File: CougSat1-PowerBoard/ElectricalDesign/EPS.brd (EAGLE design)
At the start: 91.4 x 95.8 mm, 250 parts, among them J1 PV0, J2 PV1, J3 PV2, J4 PV3, J5 Umbilical, J6 SWD, J7 CougSat Card, J8 Deployables, Q1 NTLUD3A50PZ, Q10 DMN2008LFU, Q11 DMN2008LFU, Q12 CSD25402Q3A, Q13 CSD25402Q3A, Q14 NTLUD3A50PZ, Q15 NTLUD3A50PZ, Q16 NTLUD3A50PZ, Q17 NTLUD3A50PZ, Q18 NTLUD3A50PZ, Q19 NTLUD3A50PZ, Q2 NTLUD3A50PZ, Q20 NTLUD3A50PZ, Q21 NTLUD3A50PZ, Q22 NTLUD3A50PZ, Q23 CSD25402Q3A, Q24 CSD25402Q3A, Q25 DMN53D0L, Q26 NTLUD3A50PZ, Q27 NTLUD3A50PZ, Q28 NTLUD3A50PZ, Q29 NTLUD3A50PZ, Q3 NTLUD3A50PZ, Q30 NTLUD3A50PZ, Q31 NTLUD3A50PZ, Q32 NTLUD3A50PZ, Q33 NTLUD3A50PZ, Q34 NTLUD3A50PZ, Q35 NTLUD3A50PZ, Q36 NTLUD3A50PZ, Q37 NTLUD3A50PZ, Q38 NTLUD3A50PZ, Q39 NTLUD3A50PZ, Q4 NTLUD3A50PZ, Q40 NTLUD3A50PZ, Q41 NTLUD3A50PZ, Q42 NTLUD3A50PZ, Q43 NTLUD3A50PZ, Q5 NTLUD3A50PZ, Q6 NTLUD3A50PZ, Q7 NTLUD3A50PZ, Q8 NTLUD3A50PZ, Q9 NTLUD3A50PZ, SW1 D2MQ-1-TL, U1 BQ29700, U10 LTC2499, U11 LTC2499, U12 LTC2499, U13 LTC2499, U14 MCP1501-18, U15 LTC2499, U2 BQ29700, U3 TPS64200, U4 TPS64200, U5 STM32L476RGT, U6 TCA9535R, U7 SN74LVC244AR, U8 TCA9535R, U9 LTC2499

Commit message: Updated I²C Addresses
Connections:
- net 3.3V: no longer U13.36
- net DGND: now also U12.36, U12.37, U13.37; no longer U12.38, U13.38
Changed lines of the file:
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@@
 <drawing>
 <settings>
-<setting alwaysvectorfont="yes"/>
+<setting alwaysvectorfont="no"/>
 <setting verticaltext="up"/>
 </settings>
@@
 <contactref element="C41" pad="2"/>
 <contactref element="R77" pad="1"/>
-<contactref element="U12" pad="38"/>
-<contactref element="U13" pad="38"/>
 <wire x1="21.3" y1="38.45" x2="18.9" y2="38.45" width="0.16" layer="16"/>
 <wire x1="18.9" y1="38.45" x2="18.9" y2="38.2" width="0.16" layer="16"/>
@@
 <wire x1="30.805" y1="-6.635" x2="30.8" y2="-6.635" width="0.3" layer="16"/>
 <wire x1="30.8" y1="-6.635" x2="29.8" y2="-6.635" width="0.16" layer="16"/>
+<contactref element="U12" pad="36"/>
+<contactref element="U12" pad="37"/>
+<contactref element="U13" pad="37"/>
 <wire x1="56.3" y1="28.8" x2="57.2" y2="28.15" width="0" layer="19" extent="16-16"/>
 <wire x1="55.8" y1="28.8" x2="56.3" y2="28.8" width="0" layer="19" extent="16-16"/>
@@
 <wire x1="34.14" y1="-5.575" x2="42.2" y2="-3.965" width="0" layer="19" extent="16-16"/>
 <wire x1="44.7" y1="-19.05" x2="50.8" y2="-10.465" width="0" layer="19" extent="16-16"/>
-<wire x1="43.8" y1="-18.4" x2="44.7" y2="-19.05" width="0" layer="19" extent="16-16"/>
 <wire x1="44.7" y1="-20.55" x2="44.7" y2="-19.05" width="0" layer="19" extent="16-16"/>
 <wire x1="44.7" y1="-21.55" x2="44.7" y2="-20.55" width="0" layer="19" extent="16-16"/>
-<wire x1="42.3" y1="-18.4" x2="43.8" y2="-18.4" width="0" layer="19" extent="16-16"/>
+<wire x1="43.3" y1="-18.4" x2="44.7" y2="-19.05" width="0" layer="19" extent="16-16"/>
+<wire x1="42.8" y1="-18.4" x2="43.3" y2="-18.4" width="0" layer="19" extent="16-16"/>
+<wire x1="42.3" y1="-18.4" x2="42.8" y2="-18.4" width="0" layer="19" extent="16-16"/>
 <wire x1="41.8" y1="-18.4" x2="42.3" y2="-18.4" width="0" layer="19" extent="16-16"/>
 <wire x1="41.3" y1="-18.4" x2="41.8" y2="-18.4" width="0" layer="19" extent="16-16"/>
@@
 <wire x1="34.4" y1="-36.5" x2="33.9" y2="-36.5" width="0" layer="19" extent="16-16"/>
 <wire x1="34.9" y1="-36.5" x2="34.4" y2="-36.5" width="0" layer="19" extent="16-16"/>
+<wire x1="35.9" y1="-36.5" x2="34.9" y2="-36.5" width="0" layer="19" extent="16-16"/>
 <wire x1="32.5" y1="-37.15" x2="33.4" y2="-36.5" width="0" layer="19" extent="16-16"/>
-<wire x1="36.4" y1="-36.5" x2="34.9" y2="-36.5" width="0" layer="19" extent="16-16"/>
-<wire x1="37.3" y1="-37.15" x2="36.4" y2="-36.5" width="0" layer="19" extent="16-16"/>
+<wire x1="37.3" y1="-37.15" x2="35.9" y2="-36.5" width="0" layer="19" extent="16-16"/>
 <wire x1="37.3" y1="-38.65" x2="37.3" y2="-37.15" width="0" layer="19" extent="16-16"/>
 <wire x1="37.3" y1="-39.65" x2="37.3" y2="-38.65" width="0" layer="19" extent="16-16"/>
@@
 <contactref element="C20" pad="1"/>
 <contactref element="C37" pad="1"/>
-<contactref element="U13" pad="36"/>
 <contactref element="RN19" pad="5"/>
 <contactref element="RN19" pad="8"/>
@@
 <wire x1="48.95" y1="-23.4" x2="48.235" y2="-21.5" width="0" layer="19" extent="16-16"/>
 <wire x1="35.965" y1="-34.2" x2="39.9" y2="-20.55" width="0" layer="19" extent="16-16"/>
-<wire x1="35.4" y1="-36.5" x2="35.965" y2="-34.2" width="0" layer="19" extent="16-16"/>
-<wire x1="32.5" y1="-38.65" x2="35.4" y2="-36.5" width="0" layer="19" extent="16-16"/>
+<wire x1="32.5" y1="-38.65" x2="35.965" y2="-34.2" width="0" layer="19" extent="16-16"/>
 <wire x1="27.365" y1="-36.9" x2="32.5" y2="-38.65" width="0" layer="19" extent="16-16"/>
 <wire x1="19.3" y1="-35.6" x2="27.365" y2="-36.9" width="0" layer="19" extent="16-16"/>

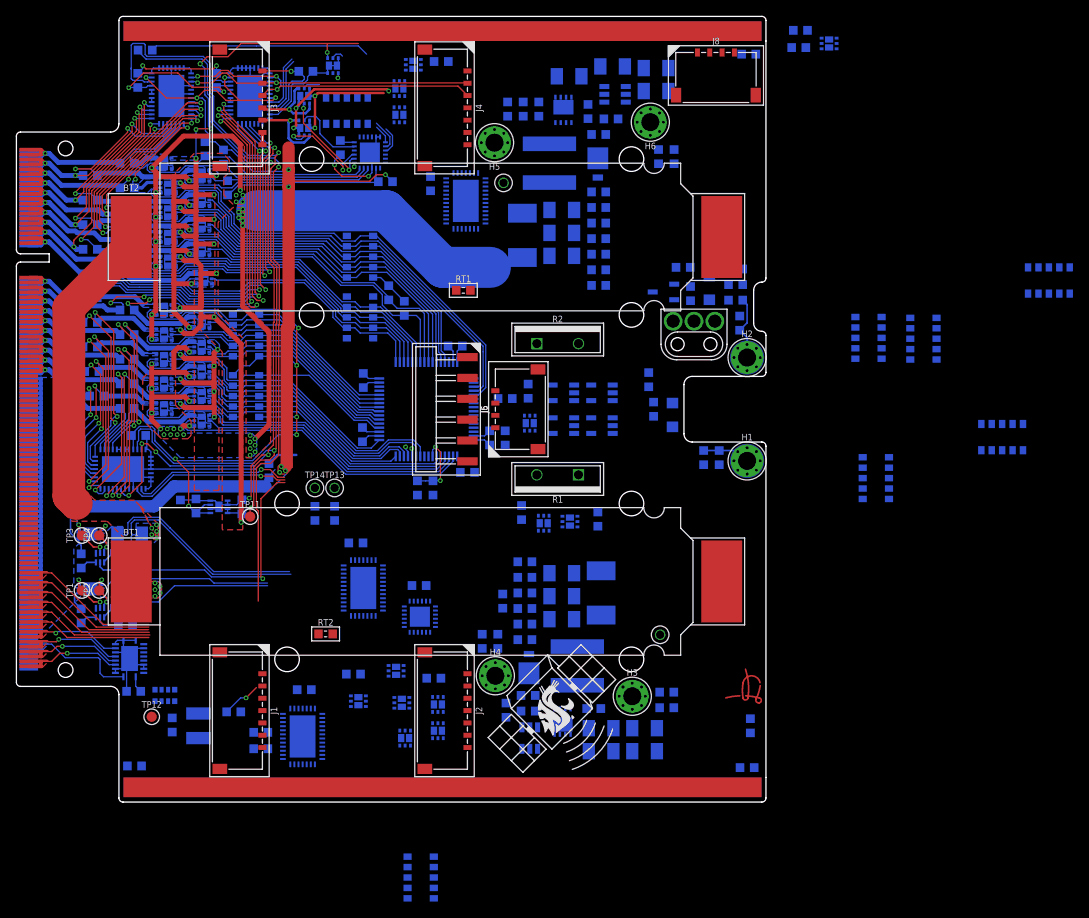
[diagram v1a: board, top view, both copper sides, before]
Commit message: Laid Out Voltage ADC
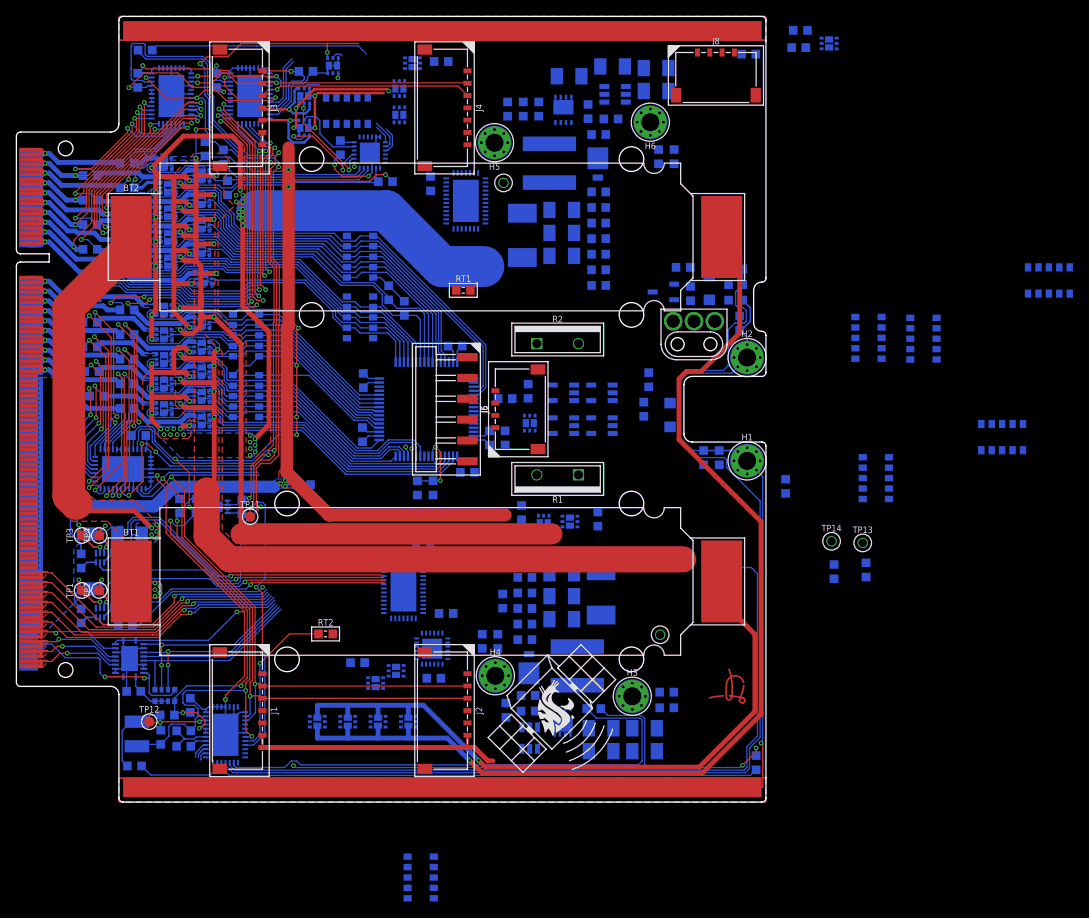
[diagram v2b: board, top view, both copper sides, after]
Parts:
- moved R72 65.2 mm to (103.6, -19.6)
- moved TP13 64.7 mm to (103.2, -16.3)
- moved R71 63.7 mm to (99.7, -19.8)
- moved TP14 63.3 mm to (99.4, -16.1)
- moved R61 29.5 mm to (93.8, -9.40), turned to 90 degrees
- moved C30 14.0 mm to (21.2, -36.1), turned to 90 degrees
- moved Q1 10.6 mm to (36.7, -38.1)
- moved R65 9.40 mm to (20.4, -41.1)
- moved R63 9.40 mm to (20.4, -39.2)
- moved U13 9.40 mm to (25.5, -39.7)
- moved C29 8.23 mm to (49.6, -17.0)
- moved FB1 8.11 mm to (18.4, -37.3)
- moved C36 7.57 mm to (14.7, -39.6)
- moved Q4 7.38 mm to (44.1, -38.1), turned to 0 degrees
- moved Q2 7.28 mm to (40.4, -38.1), turned to 0 degrees
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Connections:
- net 3.3V-A: now also U13.21
- net 3.3V-B: now also U13.22
- net AVREF: now also U13.9
- net EJECT_TIMER: now also U13.16
- net PC_DEPLOY-A: now also U5.56
- net PC_DEPLOY-B: now also U5.57
- net TEMP+X+Y: now also U13.10
- net TEMP+X-Y: now also U13.17
- net TEMP-BATT-A: now also U13.8
- net TEMP-BATT-B: now also U13.19
- net TEMP-PMIC: now also U13.12
- net TEMP-REG-A: now also U13.14
- net TEMP-REG-B: now also U13.23
- net TEMP-X+Y: now also U13.13
- net TEMP-X-Y: now also U13.18
- net UMB_IN: now also U13.11
- net UMB_SW-A: now also U5.59
- net UMB_SW-B: now also U5.58
- net VBATT-A: now also U13.15
- net VBATT-B: now also U13.20
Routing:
- net VBATT-A: track 21.4 -> 189.6 mm
- net CHASSIS: track 13.8 -> 158.4 mm, vias 0 -> 1
- net EJECT_TIMER: track 0.00 -> 140.5 mm
- net VIN-B: track 48.3 -> 174.8 mm, vias 4 -> 5
- net VIN-A: track 16.0 -> 116.7 mm, vias 2 -> 4
- net AVDD: track 87.6 -> 161.3 mm, vias 2 -> 6
- net PGND: track 221.5 -> 288.2 mm
- net TEMP+X-Y: track 0.00 -> 66.5 mm
- net TEMP-REG-A: track 0.00 -> 63.3 mm
- net DGND: track 120.1 -> 179.8 mm, vias 5 -> 8
- net I2C_SDA: track 55.5 -> 112.9 mm, vias 3 -> 4
- net AGND: track 119.3 -> 176.3 mm, vias 10 -> 13
- net I2C_SCL: track 59.4 -> 116.4 mm, vias 4 -> 5
- net 3.3V: track 106.8 -> 157.0 mm, vias 9 -> 13
- net 3.3V-A: track 113.2 -> 153.9 mm, vias 18 -> 17
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- added copper zone on layer 1, net CHASSIS

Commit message: Laid Out 3V3A Regulator
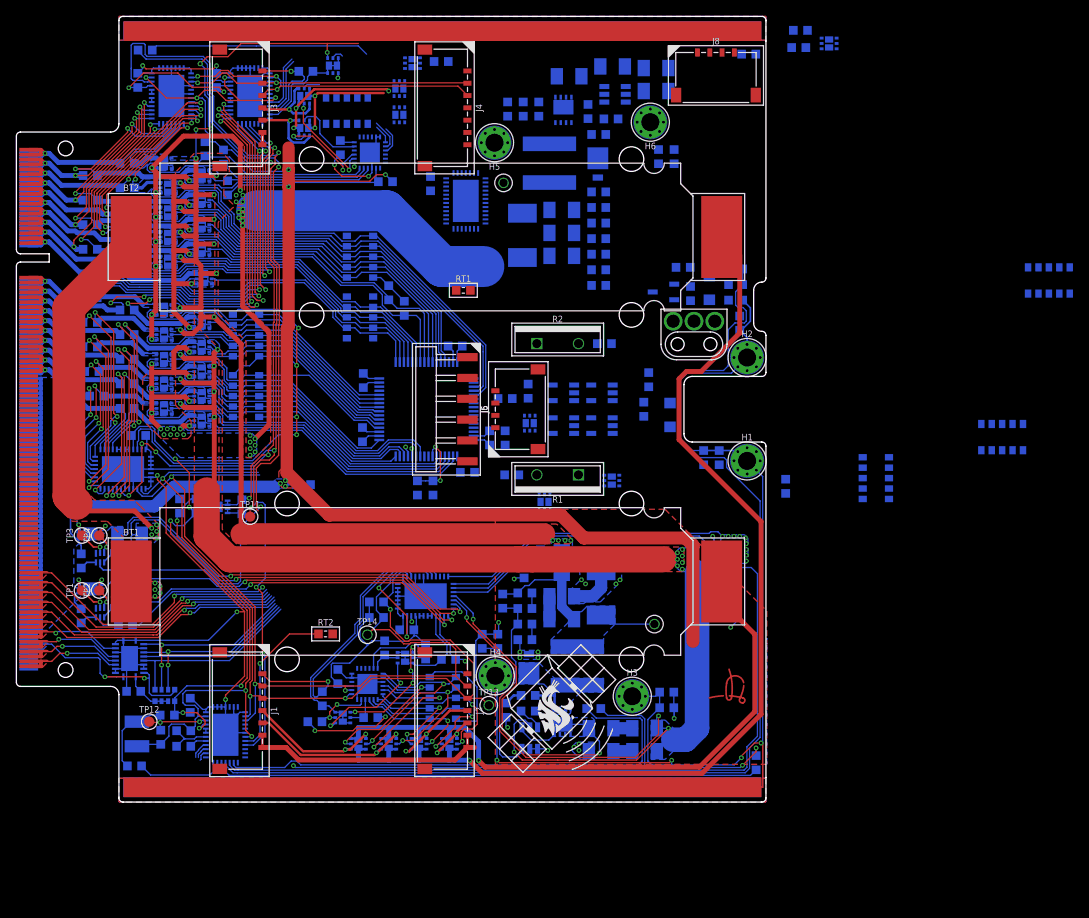
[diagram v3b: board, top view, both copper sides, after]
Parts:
- removed RN4, RN5: 10kΩ 5%, CougsInSpace-Resistors:3264
- added R86, R87, R88, R89: 10kΩ 0.1%, CougsInSpace-Resistors:1608
- moved R72 59.8 mm to (43.9, -23.5), turned to 0 degrees
- moved TP14 57.7 mm to (42.8, -27.5)
- moved R71 56.1 mm to (43.9, -25.4), turned to 0 degrees
- moved TP13 49.7 mm to (57.6, -36.1)
- moved RN20 22.1 mm to (52.0, -35.2)
- moved R57 21.4 mm to (71.7, 8.00), turned to 180 degrees
- moved C23 15.3 mm to (39.2, -32.6), turned to 90 degrees
- moved C29 10.1 mm to (47.6, -26.9)
- moved Q4 9.11 mm to (52.8, -40.8)
- moved U8 8.99 mm to (42.8, -33.5), turned to 270 degrees
- moved Q43 7.14 mm to (72.6, -8.70)
- moved R42 6.15 mm to (37.3, -35.3), turned to 270 degrees
- moved Q28 5.80 mm to (39.8, -37.6)
- moved Q1 5.68 mm to (41.7, -40.8)
- moved Q2 5.68 mm to (45.4, -40.8)
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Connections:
- net 3.3V: now also R86.2, R87.2, R88.2, R89.2; no longer RN4.10, RN4.5, RN5.10, RN5.5
- net 3.3V-A: now also U12.14
- net 3.3V_I-A: now also U12.15
- net 3.3V_ISENS-A: now also U12.16
- net BP_VSS-A: now also U12.21
- net BP_VSS-B: now also U12.19
- net BP_VSS_I-A: now also U12.20
- net BP_VSS_I-B: now also U12.18
- net I_BH-0: now also U12.11
- net PR_BH-0: now also U12.10
- net PVC_3.3V-0A: now also R86.1, U8.16
- net PVC_3.3V-0B: now also R87.1, U8.17
- net PVC_3.3V-1A: now also R88.1, U8.5
- net PVC_3.3V-1B: now also R89.1, U8.6
- net PVI_3.3V-0: now also U12.9
- net PVI_3.3V-1: now also U12.23
- net PV_3.3V-0: now also U12.8
- net PV_3.3V-1: now also U12.22
- net PV_SW-0A: now also U8.7
- net PV_SW-0B: now also RN20.9, U8.8; no longer RN20.2
- net PV_SW-1A: now also RN20.2, U8.10; no longer RN20.3
- net PV_SW-1B: now also RN20.8, U8.11; no longer RN20.4
- net PV_SW-2A: now also U8.15
- net PV_SW-2B: now also U8.13
- net PV_SW-3A: now also RN20.3, U8.12; no longer RN20.8
- net PV_SW-3B: now also RN20.4, U8.14; no longer RN20.9
- net VBATT-A: now also U12.13, U12.17
- net VIN-A: now also U12.12
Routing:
- net VBATT-A: track 189.6 -> 320.2 mm, vias 7 -> 18
- net PGND: track 288.2 -> 368.3 mm, vias 6 -> 23
- net CHASSIS: track 158.4 -> 224.0 mm, vias 1 -> 4
- net 3.3V_ISENS-A: track 0.00 -> 45.7 mm, vias 0 -> 2
- net 3.3V: track 157.0 -> 195.4 mm, vias 13 -> 15
- net 3.3V_I-A: track 0.00 -> 37.0 mm
- net PV_3.3V-0: track 0.00 -> 36.8 mm, vias 0 -> 1
- net VIN-A: track 116.7 -> 151.8 mm, vias 4 -> 13
- net PVI_3.3V-0: track 0.00 -> 33.5 mm
- net I2C_SCL: track 116.4 -> 148.3 mm, vias 5 -> 7
- net I2C_SDA: track 112.9 -> 143.0 mm, vias 4 -> 5
- net 3.3V-A: track 153.9 -> 182.5 mm, vias 17 -> 25
- net DGND: track 179.8 -> 205.7 mm
- net 3.3V_REG_FB-A: track 0.00 -> 24.4 mm
- net PV_SW-0A: track 0.00 -> 22.8 mm, vias 0 -> 2
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- added copper zone on layer 16, net 3.3V_I-A
- added copper zone on layer 16, net 3.3V_ISENS-A
- added copper zone on layer 16, net 3.3V_REG_BUCK_NODE-A
- added copper zone on layer 16, net VIN-A

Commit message: Laid Out Voltage ADC
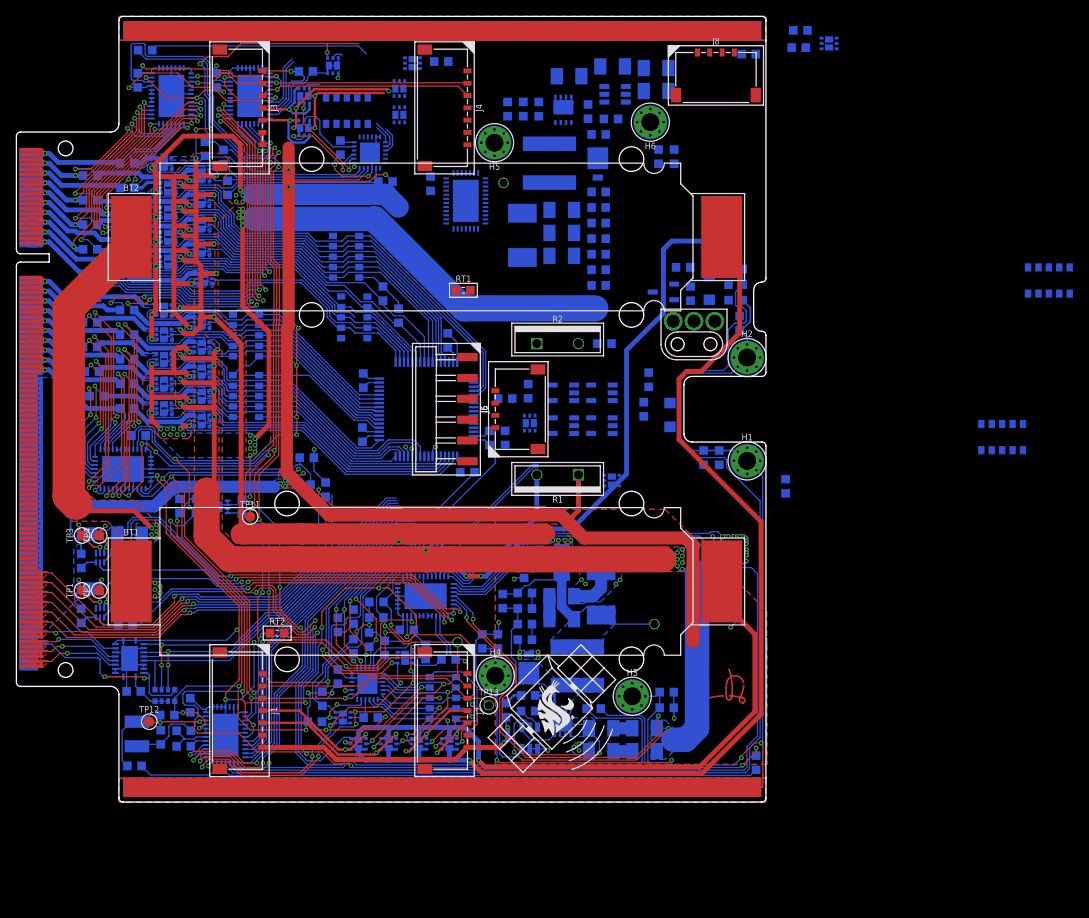
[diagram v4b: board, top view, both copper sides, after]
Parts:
- removed RN6: 10kΩ 5%, CougsInSpace-Resistors:3264
- added R90, R91, R92, R93: 10kΩ 0.1%, CougsInSpace-Resistors:1608
- TP1: value (none) -> TEST_POINT-SMD-C-1.25
- moved C22 15.8 mm to (35.4, -5.90), turned to 0 degrees
- moved Q42 14.5 mm to (51.3, -17.4)
- moved R78 11.2 mm to (37.7, -9.80)
- moved TP14 11.0 mm to (53.8, -28.4), flipped to the bottom
- moved R56 11.0 mm to (54.6, -17.3), turned to 0 degrees
- moved RT2 5.90 mm to (31.8, -27.3)
- moved RN2 1.70 mm to (40.2, 18.6)
- moved C20 1.14 mm to (52.6, 8.40), turned to 270 degrees
- moved R85 1.14 mm to (46.6, 11.4)
- moved R84 0.71 mm to (44.7, 14.1)
- moved RN10 0.70 mm to (41.2, 11.2)
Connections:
- net 3.3V: now also R90.2, R91.2, R92.2, R93.2; no longer RN6.10, RN6.5
- net 3.3V-A: now also U13.19; no longer U13.21
- net 3.3V-B: now also U13.20; no longer U13.22
- net I_BH-0: now also U12.10; no longer U12.11
- net PC_BH-0A: now also R93.1, U8.3
- net PC_BH-0B: now also R91.1, U8.4
- net PC_BH-1A: now also R90.1, U8.1
- net PC_BH-1B: now also R92.1, U8.2
- net PR_BH-0: now also U12.11; no longer U12.10
- net TEMP+X+Y: now also U13.12; no longer U13.10
- net TEMP-BATT-B: now also U13.21; no longer U13.19
- net TEMP-PMIC: now also U13.10; no longer U13.12
- net TEMP-REG-B: now also U13.22; no longer U13.23
- net VBATT-B: now also U13.23; no longer U13.20
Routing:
- net VBATT-B: track 54.1 -> 218.3 mm, vias 28 -> 35
- net 3.3V-B: track 88.1 -> 159.5 mm, vias 21 -> 25
- net UMB_IN: track 0.00 -> 56.0 mm, vias 0 -> 1
- net 3.3V-A: track 182.5 -> 236.4 mm, vias 25 -> 30
- net AVDD: track 161.3 -> 212.2 mm, vias 6 -> 10
- net TEMP-PMIC: track 0.00 -> 48.5 mm
- net TEMP-BATT-B: track 0.00 -> 48.5 mm, vias 0 -> 2
- net TEMP-REG-B: track 2.21 -> 49.7 mm, vias 0 -> 2
- net PWR_CTRL_SW: track 35.9 -> 81.0 mm, vias 1 -> 2
- net DGND: track 205.7 -> 248.4 mm, vias 8 -> 11
- net PC_BH-1A: track 0.00 -> 41.5 mm, vias 0 -> 2
- net VIN-A: track 151.8 -> 192.7 mm, vias 13 -> 14
- net PC_BH-1B: track 0.00 -> 40.9 mm, vias 0 -> 2
- net TEMP-X+Y: track 26.8 -> 67.0 mm
- net TEMP+X+Y: track 0.00 -> 39.1 mm
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- added copper zone on layer 16, net I_BH-0
- added copper zone on layer 1, net VIN-A
